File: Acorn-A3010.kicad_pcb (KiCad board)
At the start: 4 copper layers, 382 x 205 mm, 124 parts, among them IC11 HM514260AZ8, IC12 DS2401+, IC13 ARM250, IC14 4HCT574, IC15 4HCT574, IC17 0296061, IC18 0296062, IC20 74HC138, IC21 HM514260AJ8, IC22 HM514260AJ8, IC24 82C711, IC25 74HC139, IC27 74AC32, IC5 PCF8583, IC6 HM514260AZ8, IC8 74HCT14, Q3 BC849, SW1 SW_Push_DPDT, X2 32.768KHz, X4 72.0MHz, X5 25.175MHz

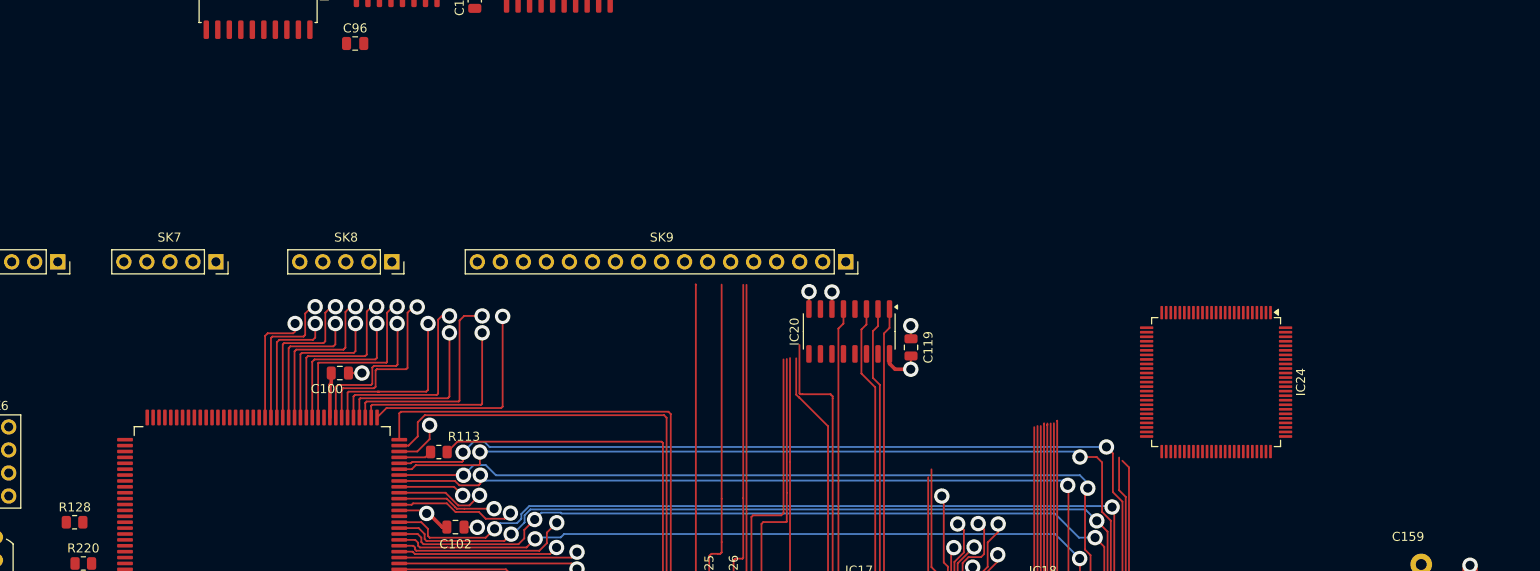
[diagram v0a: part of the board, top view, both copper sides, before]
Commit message: add io details
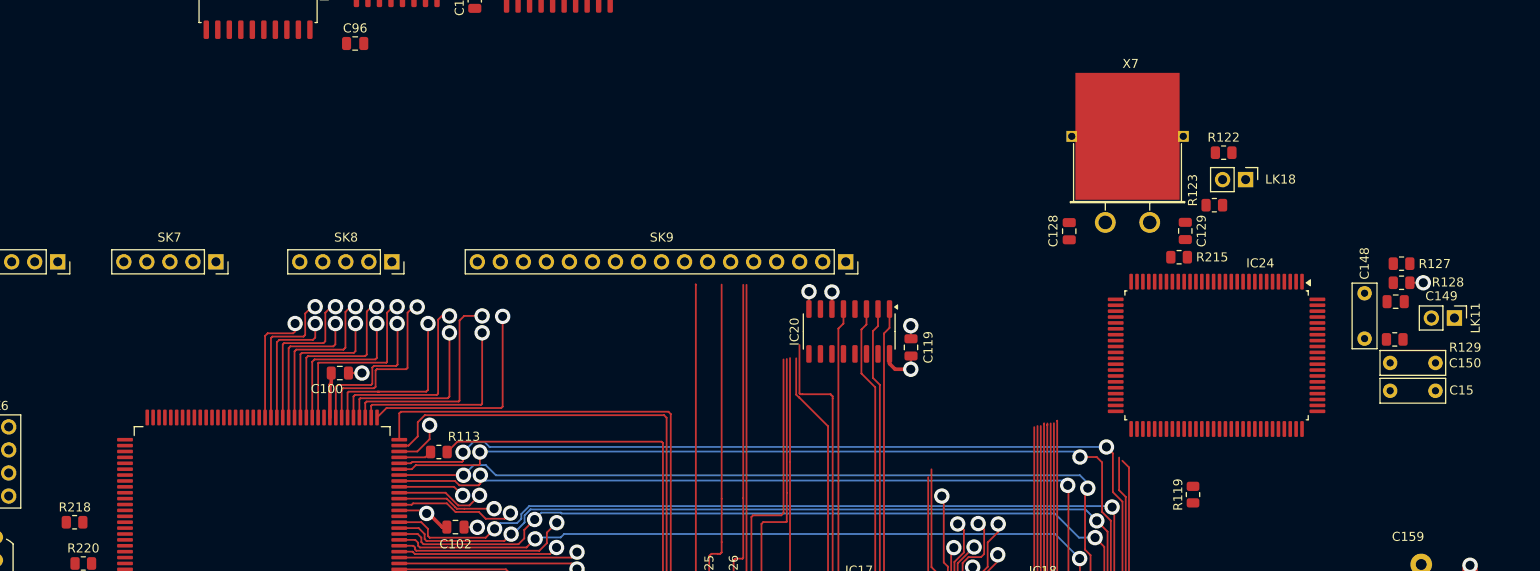
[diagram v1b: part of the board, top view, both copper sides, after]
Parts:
- added C128: 22pF, Capacitor_SMD:C_0805_2012Metric, F.Cu at (316.1, 93.2)
- added C129: 22pF, Capacitor_SMD:C_0805_2012Metric, F.Cu at (328.9, 93.2)
- added C148: 4.7nF, Capacitor_THT:C_Rect_L7.0mm_W2.5mm_P5.00mm, F.Cu at (348.7, 105.0)
- added C149: 2.7nF, Capacitor_SMD:C_0805_2012Metric, F.Cu at (352.1, 101.0)
- added C15: 4.7nF, Capacitor_THT:C_Rect_L7.0mm_W2.5mm_P5.00mm, F.Cu at (351.5, 110.8)
- added C150: 150nF 5%, Capacitor_THT:C_Rect_L7.0mm_W2.5mm_P5.00mm, F.Cu at (351.5, 107.7)
- added LK11: NF, Connector_PinHeader_2.54mm:PinHeader_1x02_P2.54mm_Vertical, F.Cu at (358.6, 102.8)
- added LK18: Pren, Connector_PinHeader_2.54mm:PinHeader_1x02_P2.54mm_Vertical, F.Cu at (335.5, 87.5)
- added R119: 10K, Resistor_SMD:R_0805_2012Metric, F.Cu at (329.7, 122.2)
- added R122: 4K7, Resistor_SMD:R_0805_2012Metric, F.Cu at (333.1, 84.5)
- added R123: 4K7, Resistor_SMD:R_0805_2012Metric, F.Cu at (332.1, 90.3)
- added R127: 6K81 1%, Resistor_SMD:R_0805_2012Metric, F.Cu at (352.7, 96.8)
- added R128: 18K2 1%, Resistor_SMD:R_0805_2012Metric, F.Cu at (352.7, 98.9)
- added R129: 1K2, Resistor_SMD:R_0805_2012Metric, F.Cu at (352.0, 105.1)
- added R215: 0R, Resistor_SMD:R_0805_2012Metric, F.Cu at (328.2, 96.1)
- added X7: 24MHz, Crystal:Crystal_HC50_Horizontal_1EP_style2, F.Cu at (325.0, 92.2)
- IC24: footprint Package_QFP:TQFP-100_14x14mm_P0.5mm -> Package_QFP:PQFP-100_14x20mm_P0.65mm
- moved IC24 2.95 mm to (332.3, 106.9)
- renumbered R128 to R218
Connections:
- IC13 pad 101: unconnected-(IC13-~{Pintr}-Pad101) -> ~{Pint}
- IC13 pad 102: unconnected-(IC13-Aen-Pad102) -> Aen
- IC13 pad 103: unconnected-(IC13-~{Ior}-Pad103) -> ~{Ior}
- IC13 pad 104: unconnected-(IC13-~{Iow}-Pad104) -> ~{Iow}
- IC13 pad 105: unconnected-(IC13-~{Dack}-Pad105) -> ~{Dack}
- IC13 pad 106: unconnected-(IC13-Tc-Pad106) -> Tc
- IC13 pad 128: unconnected-(IC13-~{Index}-Pad128) -> ~{Index}
- IC13 pad 129: unconnected-(IC13-Drq-Pad129) -> Drq
- IC13 pad 132: unconnected-(IC13-~{Fintr}-Pad132) -> ~{Fintr}
- IC13 pad 133: unconnected-(IC13-~{Sintr}-Pad133) -> ~{Sintr}
- IC24 pad 12: unconnected-(IC24-Index-Pad12) -> ~{Index}
- IC24 pad 18: unconnected-(IC24-Pren-Pad18) -> Net-(IC24-Pren)
- IC24 pad 19: unconnected-(IC24-Drvtyp-Pad19) -> Net-(IC24-Drvtyp)
- IC24 pad 20: unconnected-(IC24-Oscl/Clk-Pad20) -> Net-(IC24-Oscl/Clk)
- IC24 pad 21: unconnected-(IC24-Osc2-Pad21) -> Net-(IC24-Osc2)
- IC24 pad 35: unconnected-(IC24-Tc-Pad35) -> Tc
- IC24 pad 36: unconnected-(IC24-Dack-Pad36) -> ~{Dack}
- IC24 pad 38: unconnected-(IC24-Irq4-Pad38) -> ~{Sintr}
- IC24 pad 39: unconnected-(IC24-Pintr-Pad39) -> ~{Pint}
- IC24 pad 40: unconnected-(IC24-Fintr-Pad40) -> ~{Fintr}
- IC24 pad 44: unconnected-(IC24-Ior-Pad44) -> ~{Ior}
- IC24 pad 45: unconnected-(IC24-Iow-Pad45) -> ~{Iow}
- IC24 pad 46: unconnected-(IC24-Aen-Pad46) -> Aen
- IC24 pad 52: unconnected-(IC24-Fdrq-Pad52) -> Drq
- IC24 pad 57: unconnected-(IC24-Rst-Pad57) -> Rst
- IC24 pad 58: unconnected-(IC24-Pwrgd-Pad58) -> Net-(IC24-Pwrgd)
- IC24 pad 94: unconnected-(IC24-Fgnd500-Pad94) -> Net-(IC24-Fgnd500)
- IC24 pad 95: unconnected-(IC24-Fgnd250-Pad95) -> Net-(IC24-Fgnd250)
- IC24 pad 96: unconnected-(IC24-Filter-Pad96) -> Net-(IC24-Filter)
- IC24 pad 97: unconnected-(IC24-Rvi-Pad97) -> Net-(IC24-Rvi)
- IC24 pad 98: unconnected-(IC24-Avss-Pad98) -> Net-(IC24-Avss)
- IC24 pad 99: unconnected-(IC24-Setcur-Pad99) -> Net-(IC24-Setcur)
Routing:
- net Net-(IC24-Rvi): track 0.00 -> 1.49 mm, vias 0 -> 1

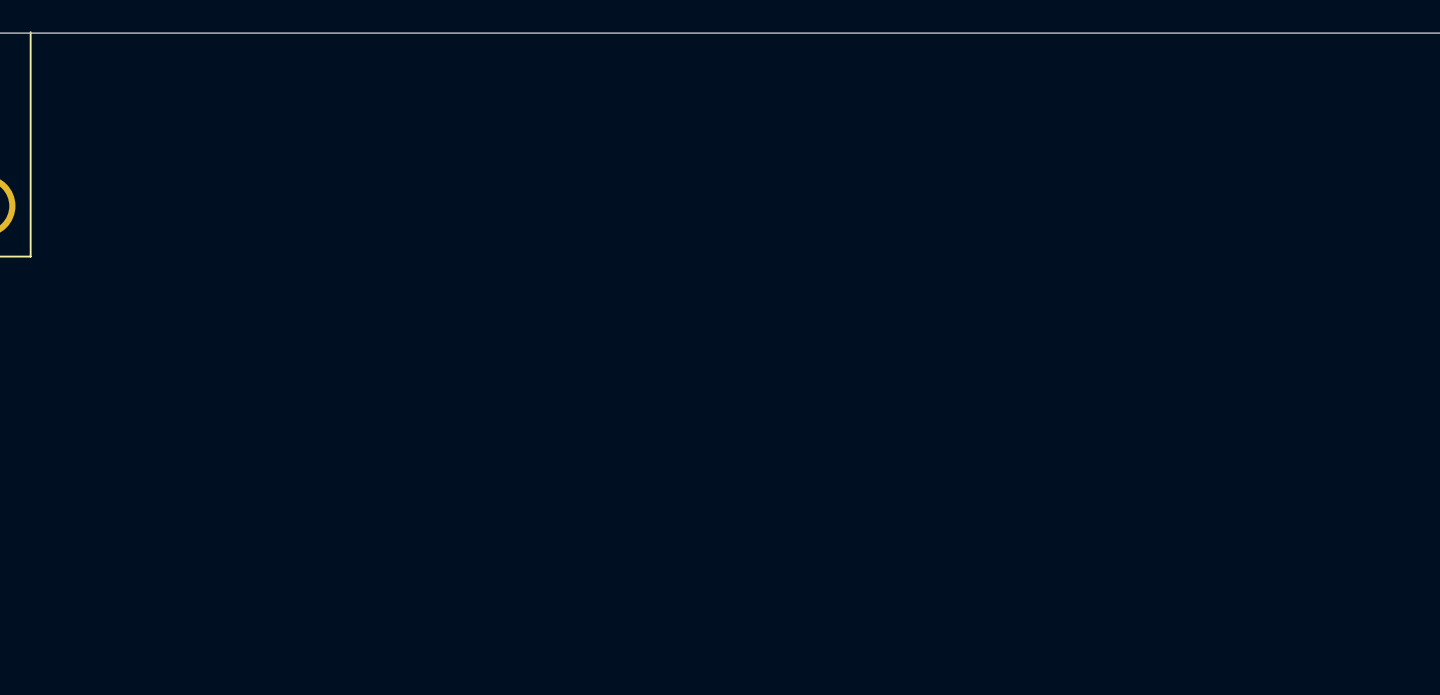
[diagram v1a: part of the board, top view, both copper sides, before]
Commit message: extend io schematic
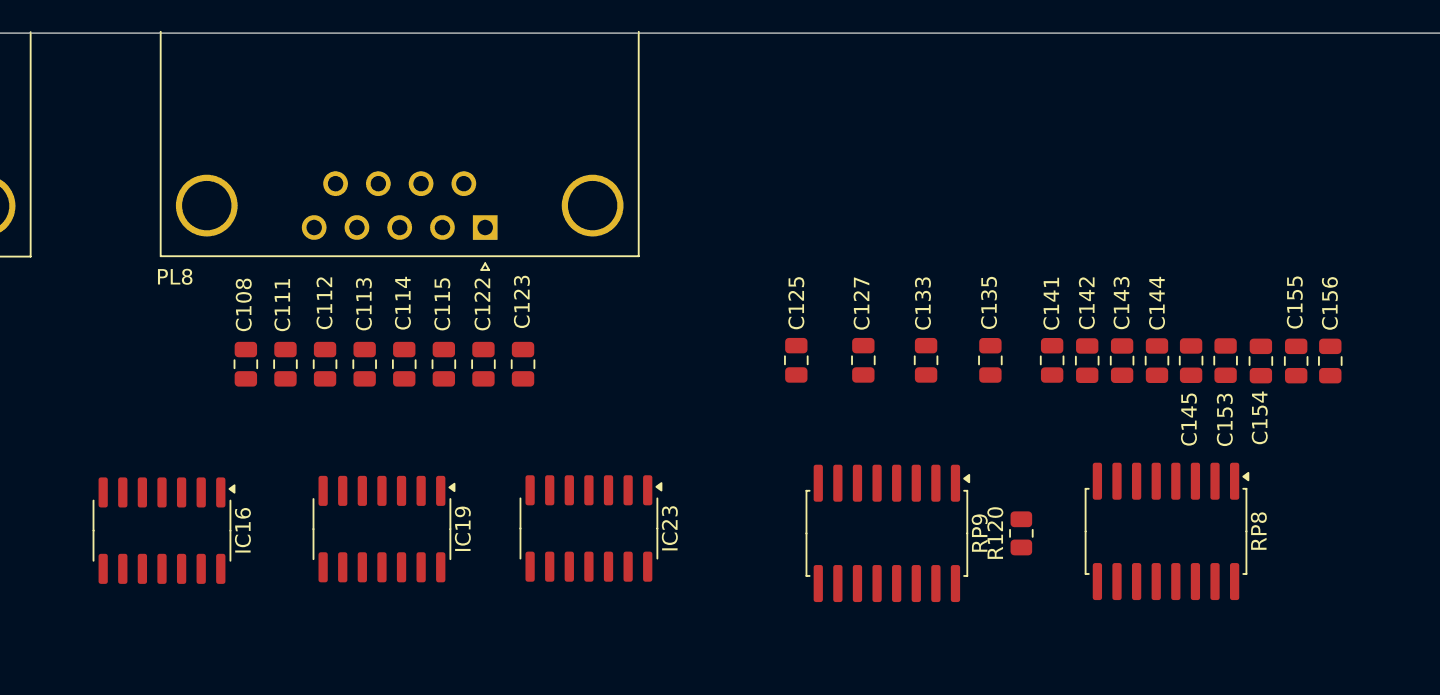
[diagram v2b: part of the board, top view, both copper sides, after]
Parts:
- added C108: 100pF, Capacitor_SMD:C_0805_2012Metric, F.Cu at (290.3, 51.1)
- added C111: 100pF, Capacitor_SMD:C_0805_2012Metric, F.Cu at (292.9, 51.1)
- added C112: 100pF, Capacitor_SMD:C_0805_2012Metric, F.Cu at (295.5, 51.1)
- added C113: 100pF, Capacitor_SMD:C_0805_2012Metric, F.Cu at (298.0, 51.1)
- added C114: 100pF, Capacitor_SMD:C_0805_2012Metric, F.Cu at (300.6, 51.1)
- added C115: 100pF, Capacitor_SMD:C_0805_2012Metric, F.Cu at (303.2, 51.1)
- added C122: 100pF, Capacitor_SMD:C_0805_2012Metric, F.Cu at (305.7, 51.1)
- added C123: 100pF, Capacitor_SMD:C_0805_2012Metric, F.Cu at (308.3, 51.1)
- added C125: 100pF, Capacitor_SMD:C_0805_2012Metric, F.Cu at (326.0, 50.8)
- added C127: 1nF, Capacitor_SMD:C_0805_2012Metric, F.Cu at (330.4, 50.8)
- added C133: 1nF, Capacitor_SMD:C_0805_2012Metric, F.Cu at (334.4, 50.8)
- added C135: 1nF, Capacitor_SMD:C_0805_2012Metric, F.Cu at (338.6, 50.8)
- added C141: 1nF, Capacitor_SMD:C_0805_2012Metric, F.Cu at (342.6, 50.8)
- added C142: 1nF, Capacitor_SMD:C_0805_2012Metric, F.Cu at (344.9, 50.9)
- added C143: 1nF, Capacitor_SMD:C_0805_2012Metric, F.Cu at (347.1, 50.9)
- added C144: 1nF, Capacitor_SMD:C_0805_2012Metric, F.Cu at (349.4, 50.9)
- added C145: 1nF, Capacitor_SMD:C_0805_2012Metric, F.Cu at (351.6, 50.9)
- added C153: 100pF, Capacitor_SMD:C_0805_2012Metric, F.Cu at (353.8, 50.9)
- added C154: 100pF, Capacitor_SMD:C_0805_2012Metric, F.Cu at (356.1, 50.9)
- added C155: 100pF, Capacitor_SMD:C_0805_2012Metric, F.Cu at (358.4, 50.9)
- added C156: 100pF, Capacitor_SMD:C_0805_2012Metric, F.Cu at (360.6, 50.9)
- added IC16: MC1489, Package_SO:SOIC-14_3.9x8.7mm_P1.27mm, F.Cu at (284.9, 61.9)
- added IC19: MC1488, Package_SO:SOIC-14_3.9x8.7mm_P1.27mm, F.Cu at (299.2, 61.8)
- added IC23: MC1489, Package_SO:SOIC-14_3.9x8.7mm_P1.27mm, F.Cu at (312.6, 61.7)
- added PL8: Serial, Connector_Dsub:DSUB-9_Male_Horizontal_P2.77x2.84mm_EdgePinOffset9.90mm_Housed_MountingHolesOffset11.32mm, F.Cu at (305.9, 42.2)
- added R120: 33R, Resistor_SMD:R_0805_2012Metric, F.Cu at (340.6, 62.1)
- added RP8: 33R, Package_SO:SOIC-16W_5.3x10.2mm_P1.27mm, F.Cu at (350.0, 61.9)
- added RP9: 33R, Package_SO:SOIC-16W_5.3x10.2mm_P1.27mm, F.Cu at (331.9, 62.1)
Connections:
- IC24 pad 59: unconnected-(IC24-Slct-Pad59) -> Net-(IC24-Slct)
- IC24 pad 60: unconnected-(IC24-Pe-Pad60) -> Net-(IC24-Pe)
- IC24 pad 61: unconnected-(IC24-Busy-Pad61) -> Net-(IC24-Busy)
- IC24 pad 62: unconnected-(IC24-Ack-Pad62) -> Net-(IC24-Ack)
- IC24 pad 63: unconnected-(IC24-Pd7-Pad63) -> Net-(IC24-Pd7)
- IC24 pad 64: unconnected-(IC24-Pd6-Pad64) -> Net-(IC24-Pd6)
- IC24 pad 65: unconnected-(IC24-Pd5-Pad65) -> Net-(IC24-Pd5)
- IC24 pad 66: unconnected-(IC24-Pd4-Pad66) -> Net-(IC24-Pd4)
- IC24 pad 68: unconnected-(IC24-Pd3-Pad68) -> Net-(IC24-Pd3)
- IC24 pad 69: unconnected-(IC24-Pd2-Pad69) -> Net-(IC24-Pd2)
- IC24 pad 70: unconnected-(IC24-Pd1-Pad70) -> Net-(IC24-Pd1)
- IC24 pad 71: unconnected-(IC24-Pd0-Pad71) -> Net-(IC24-Pd0)
- IC24 pad 73: unconnected-(IC24-Sictin-Pad73) -> Net-(IC24-Sictin)
- IC24 pad 74: unconnected-(IC24-Init-Pad74) -> Net-(IC24-Init)
- IC24 pad 75: unconnected-(IC24-Error-Pad75) -> Net-(IC24-Error)
- IC24 pad 76: unconnected-(IC24-Autofd-Pad76) -> Net-(IC24-Autofd)
- IC24 pad 77: unconnected-(IC24-Strobe-Pad77) -> Net-(IC24-Strobe)
- IC24 pad 78: unconnected-(IC24-Rxd1-Pad78) -> Net-(IC23B-OutputB)
- IC24 pad 79: unconnected-(IC24-Txd1-Pad79) -> Net-(IC19B-InputB2)
- IC24 pad 80: unconnected-(IC24-Dsr1-Pad80) -> Net-(IC16A-OutputA)
- IC24 pad 81: unconnected-(IC24-Rts1-Pad81) -> Net-(IC19D-InputD2)
- IC24 pad 82: unconnected-(IC24-Cts1-Pad82) -> Net-(IC16D-OutputD)
- IC24 pad 83: unconnected-(IC24-Dtr1-Pad83) -> Net-(IC19C-InputC2)
- IC24 pad 84: unconnected-(IC24-Ri1-Pad84) -> Net-(IC16C-OutputC)
- IC24 pad 85: unconnected-(IC24-Dcd1-Pad85) -> Net-(IC23A-OutputA)

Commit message: progress schematic
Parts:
- added C126: 100pF, Capacitor_SMD:C_0805_2012Metric, F.Cu at (326.1, 52.0)
- added C132: 100pF, Capacitor_SMD:C_0805_2012Metric, F.Cu at (330.4, 52.0)
- added C134: 100pF, Capacitor_SMD:C_0805_2012Metric, F.Cu at (334.8, 52.0)
- added C136: 100pF, Capacitor_SMD:C_0805_2012Metric, F.Cu at (339.1, 52.0)
- added C146: 33nF, Capacitor_SMD:C_0805_2012Metric, F.Cu at (343.5, 58.8)
- added C147: 100nF, Capacitor_SMD:C_0805_2012Metric, F.Cu at (352.7, 93.7)
- added C157: 47uF, Capacitor_THT:CP_Radial_D8.0mm_P5.00mm, F.Cu at (363.9, 65.2)
- added C158: 100nF, Capacitor_SMD:C_0805_2012Metric, F.Cu at (357.1, 77.1)
- added C60: 100uF, Capacitor_THT:CP_Radial_D8.0mm_P5.00mm, F.Cu at (170.9, 51.9)
- added C62: 47uF, Capacitor_THT:CP_Radial_D8.0mm_P5.00mm, F.Cu at (167.8, 62.8)
- added C68: 100uF, Capacitor_THT:CP_Radial_D8.0mm_P5.00mm, F.Cu at (177.4, 60.4)
- added C77: 33nF, Capacitor_SMD:C_0805_2012Metric, F.Cu at (199.3, 53.3)
- added C79: 33nF, Capacitor_SMD:C_0805_2012Metric, F.Cu at (188.5, 85.1)
- added C80: 47uF, Capacitor_THT:CP_Radial_D8.0mm_P5.00mm, F.Cu at (199.2, 91.6)
- added C86: 47uF, Capacitor_THT:CP_Radial_D8.0mm_P5.00mm, F.Cu at (208.6, 53.9)
- added C87: 33nF, Capacitor_SMD:C_0805_2012Metric, F.Cu at (260.0, 111.0)
- added C88: 10uF, Capacitor_THT:CP_Radial_D4.0mm_P2.00mm, F.Cu at (205.6, 85.5)
- added C89: 33nF, Capacitor_SMD:C_0805_2012Metric, F.Cu at (205.6, 88.7)
- added C90: 10uF, Capacitor_THT:CP_Radial_D4.0mm_P2.00mm, F.Cu at (207.9, 92.9)
- added C93: 10uF, Capacitor_THT:CP_Radial_D4.0mm_P2.00mm, F.Cu at (216.8, 88.0)
- added D20: BAT, Package_TO_SOT_SMD:SOT-23-3, F.Cu at (210.3, 87.6)
- added D21: BAT, Package_TO_SOT_SMD:SOT-23-3, F.Cu at (260.2, 108.0)
- added FS5: 0A25, Fuse:Fuse_1206_3216Metric, F.Cu at (201.6, 50.0)
- added IC2: 80C51, Package_LCC:PLCC-44_16.6x16.6mm_P1.27mm, F.Cu at (137.6, 216.3)
- added IC3: 74LS145, Package_SO:SOIC-16_3.9x9.9mm_P1.27mm, F.Cu at (143.0, 179.3)
- added IC4: 74LS145, Package_SO:SOIC-16_3.9x9.9mm_P1.27mm, F.Cu at (142.8, 194.3)
- added IC7: 74LS366, Package_SO:SOIC-16_3.9x9.9mm_P1.27mm, F.Cu at (173.3, 220.0)
- added IC9: 74LS241, Package_SO:SOIC-20W_7.5x12.8mm_P1.27mm, F.Cu at (190.9, 54.2)
- added IM2: Audio Hybrid, Connector_PinSocket_2.54mm:PinSocket_1x19_P2.54mm_Vertical, F.Cu at (180.4, 80.2)
- added L14: 2R2, Acorn:L_Acorn_8x3mm, F.Cu at (353.9, 81.0)
- added LK10: ID4, Connector_PinHeader_2.54mm:PinHeader_1x02_P2.54mm_Vertical, F.Cu at (150.6, 178.2)
- added LK12: ID0, Connector_PinHeader_2.54mm:PinHeader_1x02_P2.54mm_Vertical, F.Cu at (150.6, 186.9)
- added LK17: Filter Ground, Connector_PinHeader_2.54mm:PinHeader_1x02_P2.54mm_Vertical, F.Cu at (187.9, 89.0)
- added LK4: ID3, Connector_PinHeader_2.54mm:PinHeader_1x02_P2.54mm_Vertical, F.Cu at (150.6, 175.7)
- added LK5: ID2, Connector_PinHeader_2.54mm:PinHeader_1x02_P2.54mm_Vertical, F.Cu at (150.6, 184.4)
- added LK7: Conn_01x02_Pin, Connector_PinHeader_2.54mm:PinHeader_1x02_P2.54mm_Vertical, F.Cu at (132.3, 179.5)
- added LK8: ID1, Connector_PinHeader_2.54mm:PinHeader_1x02_P2.54mm_Vertical, F.Cu at (150.6, 189.5)
- added LK9: ID5, Connector_PinHeader_2.54mm:PinHeader_1x02_P2.54mm_Vertical, F.Cu at (150.6, 180.8)
- added PL9: 34WAYBOXPLUG, Connector_IDC:IDC-Header_2x17_P2.54mm_Vertical, F.Cu at (388.4, 67.0)
- added R116: 4K7, Resistor_SMD:R_0805_2012Metric, F.Cu at (321.0, 59.2)
- added R117: 4K7, Resistor_SMD:R_0805_2012Metric, F.Cu at (323.1, 59.2)
- added R118: 4K7, Resistor_SMD:R_0805_2012Metric, F.Cu at (325.3, 59.2)
- added R121: 4K7, Resistor_SMD:R_0805_2012Metric, F.Cu at (341.3, 58.8)
- added R126: 4K7, Resistor_SMD:R_0805_2012Metric, F.Cu at (351.0, 46.4)
- added R131: 4K7, Resistor_SMD:R_0805_2012Metric, F.Cu at (353.2, 46.4)
- added R138: 4K7, Resistor_SMD:R_0805_2012Metric, F.Cu at (381.2, 68.3)
- added R139: 1K, Resistor_SMD:R_0805_2012Metric, F.Cu at (381.2, 75.8)
- added R140: 4K7, Resistor_SMD:R_0805_2012Metric, F.Cu at (381.2, 78.3)
- added R141: 4K7, Resistor_SMD:R_0805_2012Metric, F.Cu at (381.2, 86.0)
- added R142: 1K, Resistor_SMD:R_0805_2012Metric, F.Cu at (381.2, 98.7)
- added R143: 1K, Resistor_SMD:R_0805_2012Metric, F.Cu at (381.2, 101.3)
- added R144: 1K, Resistor_SMD:R_0805_2012Metric, F.Cu at (381.2, 103.9)
- added R145: 1K, Resistor_SMD:R_0805_2012Metric, F.Cu at (381.2, 109.0)
- added R212: 3K3, Resistor_SMD:R_0805_2012Metric, F.Cu at (218.8, 76.6)
- added R49: 4K7, Resistor_SMD:R_0805_2012Metric, F.Cu at (154.8, 213.0)
- added R71: 330R, Resistor_SMD:R_0805_2012Metric, F.Cu at (175.1, 116.4)
- added R72: 330R, Resistor_SMD:R_0805_2012Metric, F.Cu at (182.8, 122.4)
- added R77: 220R, Resistor_SMD:R_0805_2012Metric, F.Cu at (171.2, 212.2)
- added R78: 270R, Resistor_SMD:R_0805_2012Metric, F.Cu at (174.1, 212.2)
- added R80: 270R, Resistor_SMD:R_0805_2012Metric, F.Cu at (180.3, 225.5)
- added R96: 22K, Resistor_SMD:R_0805_2012Metric, F.Cu at (210.4, 84.5)
- added RP3: 47K, Package_SO:SOIC-16W_5.3x10.2mm_P1.27mm, F.Cu at (129.1, 194.5)
- added SK10: Printer, Connector_Dsub:DSUB-25_Female_Horizontal_P2.77x2.84mm_EdgePinOffset9.90mm_Housed_MountingHolesOffset11.32mm, F.Cu at (325.8, 42.3)
- added SK2: 20WAYFLEX, Connector_PinHeader_2.54mm:PinHeader_1x20_P2.54mm_Vertical, F.Cu at (178.1, 120.2)
- added SK3: 20WAYFLEX, Connector_PinHeader_2.54mm:PinHeader_1x20_P2.54mm_Vertical, F.Cu at (129.8, 124.4)
- added SK6: Keyboard, Acorn:Mini-DIN_9, F.Cu at (191.3, 48.9)
- moved C3 9.96 mm to (157.4, 213.2)
- moved LK3 9.96 mm to (162.6, 219.8)
- moved PL8 4.62 mm to (301.2, 42.3)
- moved R120 3.56 mm to (339.1, 58.8)
- moved C112 3.13 mm to (292.4, 51.5)
- moved C113 3.13 mm to (294.9, 51.5)
- moved C123 3.13 mm to (305.2, 51.5)
- moved IC19 3.13 mm to (296.1, 62.2)
- moved IC23 3.13 mm to (309.5, 62.2)
- moved C108 3.13 mm to (287.2, 51.5)
- moved C111 3.13 mm to (289.8, 51.5)
- moved C114 3.13 mm to (297.5, 51.5)
- moved C115 3.13 mm to (300.1, 51.5)
- moved C122 3.13 mm to (302.6, 51.5)
- moved IC16 3.13 mm to (281.8, 62.3)
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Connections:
- IC16 pad 14: unconnected-(IC16E-VCC-Pad14) -> +5C
- IC19 pad 14: unconnected-(IC19E-VCC-Pad14) -> +5C
- IC23 pad 14: unconnected-(IC23E-VCC-Pad14) -> +5C
- IC24 pad 1: unconnected-(IC24-Rpm/Lc-Pad1) -> /IO/Density
- IC24 pad 10: unconnected-(IC24-Wgate-Pad10) -> /IO/~{Writegate}
- IC24 pad 100: unconnected-(IC24-Avcc-Pad100) -> Net-(IC24-Avcc)
- IC24 pad 11: unconnected-(IC24-Hdsel-Pad11) -> /IO/~{Side1}
- IC24 pad 13: unconnected-(IC24-Trk0-Pad13) -> /IO/~{Track00}
- IC24 pad 14: unconnected-(IC24-Wrprt-Pad14) -> /IO/~{Writeprot}
- IC24 pad 16: unconnected-(IC24-Rddata-Pad16) -> /IO/~{Readdata}
- IC24 pad 17: unconnected-(IC24-Dskchg-Pad17) -> /IO/DC
- IC24 pad 2: unconnected-(IC24-Mtr0-Pad2) -> /IO/~{MotorOn}
- IC24 pad 4: unconnected-(IC24-Drv0-Pad4) -> ~{Sel0}
- IC24 pad 7: unconnected-(IC24-Dir-Pad7) -> /IO/~{Dirin}
- IC24 pad 8: unconnected-(IC24-Step-Pad8) -> /IO/~{Step}
- IC24 pad 9: unconnected-(IC24-Wrdata-Pad9) -> /IO/~{Writedata}
- R120 pad 2: unconnected-(R120-Pad2) -> Net-(C136-Pad1)
- RP9 pad 4: unconnected-(RP9-R4.1-Pad4) -> Net-(RP9-R4.1)
- RP9 pad 7: unconnected-(RP9-R7.1-Pad7) -> Net-(RP9-R7.1)
- RP9 pad 8: unconnected-(RP9-R8.1-Pad8) -> Net-(RP9-R8.1)
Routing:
- net Net-(D15-K): track 403.7 -> 351.0 mm
- net +5V: track 101.2 -> 129.2 mm, vias 23 -> 25
- net /IO/Density: track 0.00 -> 9.38 mm
- net /IO/DC: track 0.00 -> 9.36 mm
- net ~{Sel0}: track 0.00 -> 9.34 mm
- net /IO/~{Readdata}: track 0.00 -> 9.34 mm
- net ~{Index}: track 0.00 -> 9.31 mm
- net /IO/~{Writeprot}: track 0.00 -> 9.31 mm
- net /IO/~{Track00}: track 0.00 -> 9.31 mm
- net /IO/~{MotorOn}: track 0.00 -> 9.29 mm
- net +5C: track 0.00 -> 2.98 mm, vias 0 -> 2
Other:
- board text added: "E"
- board text added: "N"
- board text added: "S"
- board text added: "W"
